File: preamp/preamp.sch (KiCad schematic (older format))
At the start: 21 parts

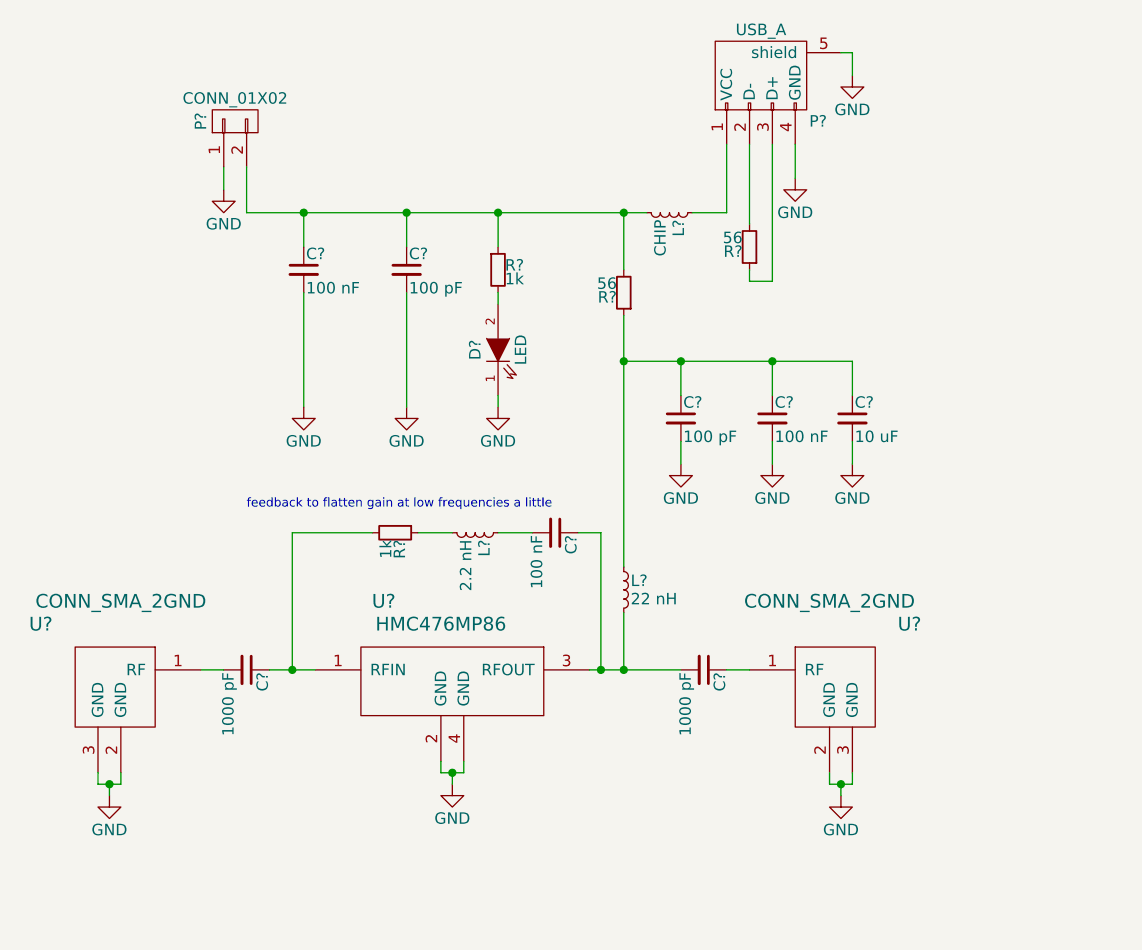
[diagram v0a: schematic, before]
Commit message: finished component placement for preamp
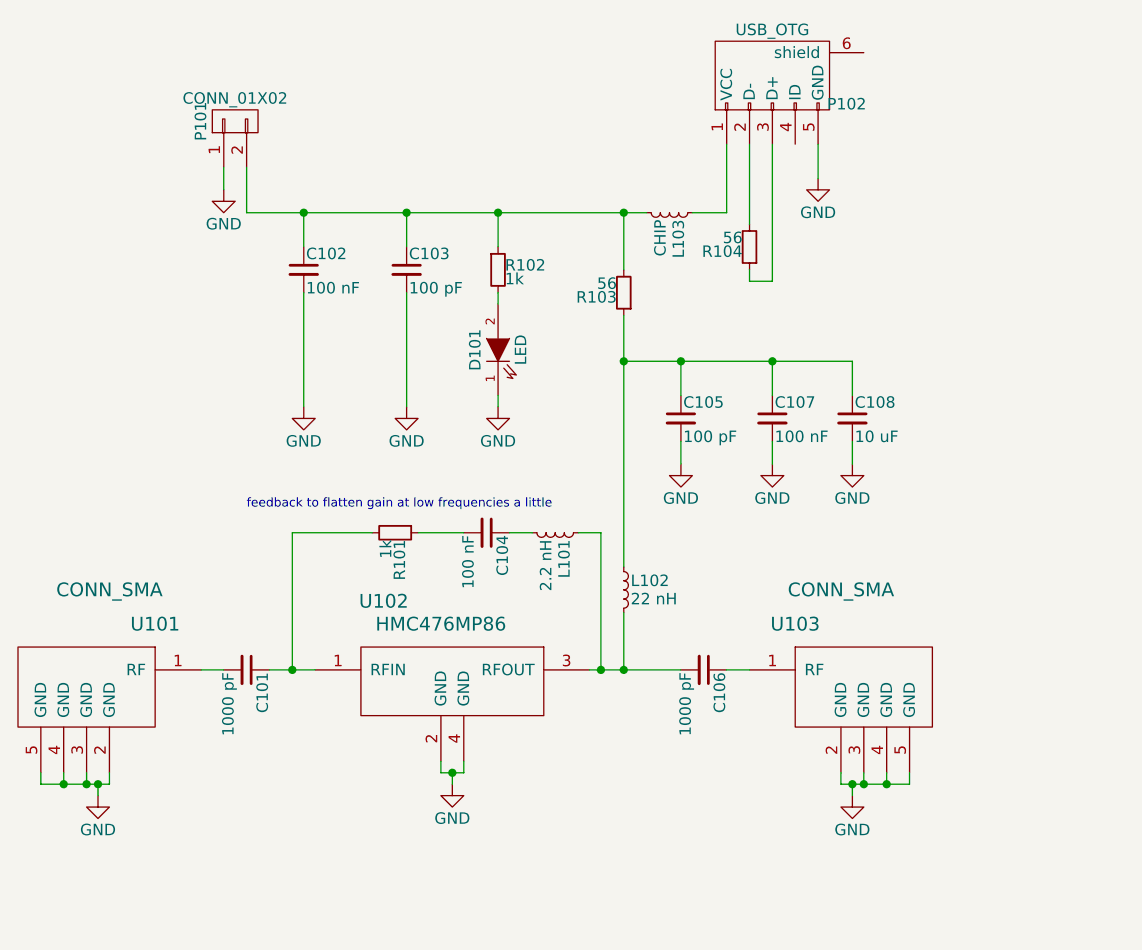
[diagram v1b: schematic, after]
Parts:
- removed P?: USB_A, symbol USB_A
- removed U? (x2): CONN_SMA_2GND, symbol CONN_SMA_2GND
- added P102: USB_OTG, Connect:USB_Micro-B_10103594-0001LF, symbol USB_OTG
- added U101, U103: CONN_SMA, vna_footprints:732512200_SMA, symbol CONN_SMA
- C101, C102, C103, C104, C105, C106, C107: renamed from C?; footprint (none) -> Capacitors_SMD:C_0402
- C108: renamed from C?; footprint (none) -> Capacitors_SMD:C_0603
- D101: renamed from D?; footprint (none) -> LEDs:LED_0603
- L101, L102: renamed from L?; footprint (none) -> Resistors_SMD:R_0402
- L103: renamed from L?; footprint (none) -> Resistors_SMD:R_0603
- P101: renamed from P?; footprint (none) -> Pin_Headers:Pin_Header_Straight_1x02
- R101, R102, R103, R104: renamed from R?; footprint (none) -> Resistors_SMD:R_0402
- U102: renamed from U?; footprint (none) -> probe_footprints:sot86
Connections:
- net GND: now also P102.5 (GND), U101.2 (GND), U101.3 (GND), U101.4 (GND), U101.5 (GND), U103.2 (GND), U103.3 (GND), U103.4 (GND), U103.5 (GND)
- net at C101.2: now also U101.1 (RF)
- net at C106.1: now also U103.1 (RF)
- net at C106.2, L102.2, U102.3 (RFOUT): now also L101.1; no longer C104.1
- net at R101.1: now also C104.2; no longer L101.2
- net at L103.1: now also P102.1 (VCC)
- net at R104.2: now also P102.2 (D-)
- net at R104.1: now also P102.3 (D+)
- new net: C104.1, L101.2
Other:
- moved on the sheet: C104, L101

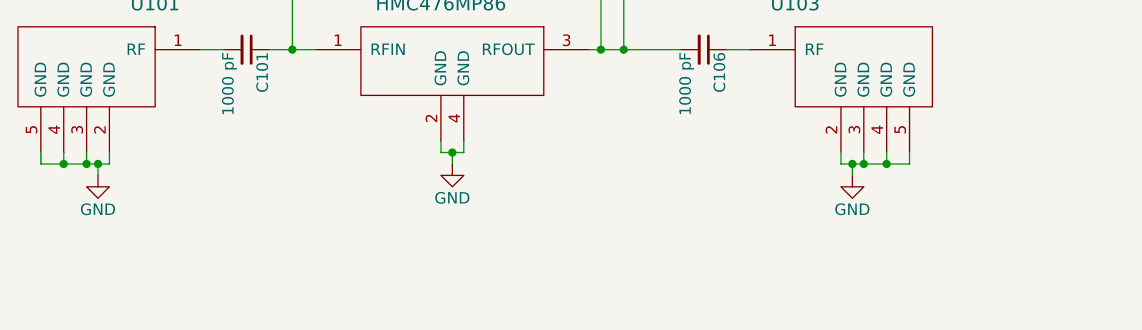
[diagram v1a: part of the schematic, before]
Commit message: added layout for preamp
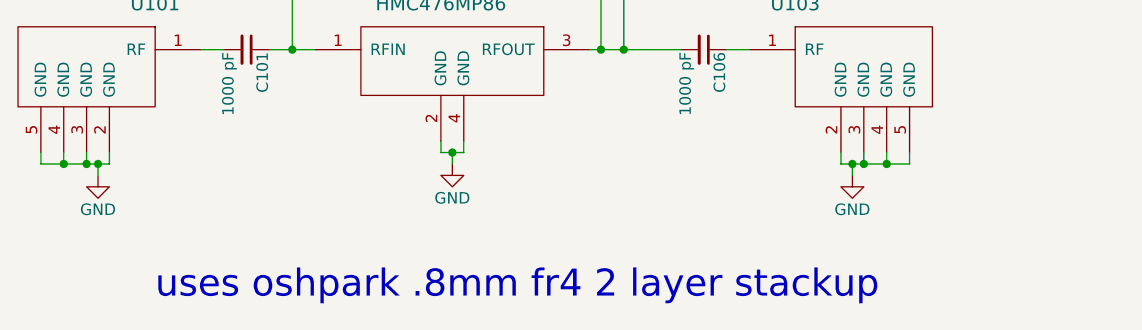
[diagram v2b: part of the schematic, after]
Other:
- note added: "uses oshpark .8mm fr4 2 layer stackup"
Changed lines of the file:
@@
 Wire Wire Line
 	4850 2800 4950 2800
+Text Notes 3300 4500 0    118  ~ 0
+uses oshpark .8mm fr4 2 layer stackup
 $EndSCHEMATC
